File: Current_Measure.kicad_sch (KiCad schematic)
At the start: 4 parts, among them U701 TMCS1101A2UQDT

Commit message: progress on CORE pcb
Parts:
- renumbered C703 to C401, C701 to C402, C702 to C403, U701 to U401
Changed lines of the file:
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@@
 		(on_board yes)
 		(dnp no)
-		(property "Reference" "#PWR0704"
+		(property "Reference" "#PWR0159"
 			(at 157.48 77.47 0)
 			(effects
@@
 			(project "EPS_CORE"
 				(path "/43e5e7c8-e7e0-4528-9a3e-b1557849918d/136d551b-dd5b-42cc-aebd-902cdeeb5d77"
-					(reference "#PWR?")
-					(unit 1)
-				)
-				(path "/43e5e7c8-e7e0-4528-9a3e-b1557849918d/1f66afe8-8069-477a-b3b2-ff8bbac6c1ca"
-					(reference "#PWR?")
+					(reference "#PWR0385")
 					(unit 1)
 				)
 				(path "/43e5e7c8-e7e0-4528-9a3e-b1557849918d/4a53a7b5-59e4-4f40-8227-8276b52a2733"
-					(reference "#PWR?")
+					(reference "#PWR0390")
 					(unit 1)
 				)
 				(path "/43e5e7c8-e7e0-4528-9a3e-b1557849918d/f6059815-62c9-4cb7-94c7-be1aeb1b1210"
-					(reference "#PWR?")
-					(unit 1)
-				)
-				(path "/43e5e7c8-e7e0-4528-9a3e-b1557849918d/f6f0c074-7c68-400b-94dc-3cfae9faea19"
-					(reference "#PWR?")
+					(reference "#PWR0159")
 					(unit 1)
 				)
@@
 		(dnp no)
 		(fields_autoplaced yes)
-		(property "Reference" "#PWR0702"
+		(property "Reference" "#PWR0160"
 			(at 143.51 115.57 0)
 			(effects
@@
 			(project "EPS_CORE"
 				(path "/43e5e7c8-e7e0-4528-9a3e-b1557849918d/136d551b-dd5b-42cc-aebd-902cdeeb5d77"
-					(reference "#PWR?")
-					(unit 1)
-				)
-				(path "/43e5e7c8-e7e0-4528-9a3e-b1557849918d/1f66afe8-8069-477a-b3b2-ff8bbac6c1ca"
-					(reference "#PWR?")
+					(reference "#PWR0386")
 					(unit 1)
 				)
 				(path "/43e5e7c8-e7e0-4528-9a3e-b1557849918d/4a53a7b5-59e4-4f40-8227-8276b52a2733"
-					(reference "#PWR?")
+					(reference "#PWR0391")
 					(unit 1)
 				)
 				(path "/43e5e7c8-e7e0-4528-9a3e-b1557849918d/f6059815-62c9-4cb7-94c7-be1aeb1b1210"
-					(reference "#PWR?")
-					(unit 1)
-				)
-				(path "/43e5e7c8-e7e0-4528-9a3e-b1557849918d/f6f0c074-7c68-400b-94dc-3cfae9faea19"
-					(reference "#PWR?")
+					(reference "#PWR0160")
 					(unit 1)
 				)
@@
 		(on_board yes)
 		(dnp no)
-		(property "Reference" "C701"
+		(property "Reference" "C402"
 			(at 140.97 91.4462 0)
 			(effects
@@
 			(project "EPS_CORE"
 				(path "/43e5e7c8-e7e0-4528-9a3e-b1557849918d/136d551b-dd5b-42cc-aebd-902cdeeb5d77"
-					(reference "C?")
-					(unit 1)
-				)
-				(path "/43e5e7c8-e7e0-4528-9a3e-b1557849918d/1f66afe8-8069-477a-b3b2-ff8bbac6c1ca"
-					(reference "C?")
+					(reference "C1702")
 					(unit 1)
 				)
 				(path "/43e5e7c8-e7e0-4528-9a3e-b1557849918d/4a53a7b5-59e4-4f40-8227-8276b52a2733"
-					(reference "C?")
+					(reference "C1802")
 					(unit 1)
 				)
 				(path "/43e5e7c8-e7e0-4528-9a3e-b1557849918d/f6059815-62c9-4cb7-94c7-be1aeb1b1210"
-					(reference "C?")
-					(unit 1)
-				)
-				(path "/43e5e7c8-e7e0-4528-9a3e-b1557849918d/f6f0c074-7c68-400b-94dc-3cfae9faea19"
-					(reference "C?")
+					(reference "C402")
 					(unit 1)
 				)
@@
 		(dnp no)
 		(fields_autoplaced yes)
-		(property "Reference" "#PWR0705"
+		(property "Reference" "#PWR0162"
 			(at 157.48 110.49 0)
 			(effects
@@
 			(project "EPS_CORE"
 				(path "/43e5e7c8-e7e0-4528-9a3e-b1557849918d/136d551b-dd5b-42cc-aebd-902cdeeb5d77"
-					(reference "#PWR?")
-					(unit 1)
-				)
-				(path "/43e5e7c8-e7e0-4528-9a3e-b1557849918d/1f66afe8-8069-477a-b3b2-ff8bbac6c1ca"
-					(reference "#PWR?")
+					(reference "#PWR0388")
 					(unit 1)
 				)
 				(path "/43e5e7c8-e7e0-4528-9a3e-b1557849918d/4a53a7b5-59e4-4f40-8227-8276b52a2733"
-					(reference "#PWR?")
+					(reference "#PWR0393")
 					(unit 1)
 				)
 				(path "/43e5e7c8-e7e0-4528-9a3e-b1557849918d/f6059815-62c9-4cb7-94c7-be1aeb1b1210"
-					(reference "#PWR?")
-					(unit 1)
-				)
-				(path "/43e5e7c8-e7e0-4528-9a3e-b1557849918d/f6f0c074-7c68-400b-94dc-3cfae9faea19"
-					(reference "#PWR?")
+					(reference "#PWR0162")
 					(unit 1)
 				)
@@
 		(dnp no)
 		(fields_autoplaced yes)
-		(property "Reference" "U701"
+		(property "Reference" "U401"
 			(at 159.6233 81.28 0)
 			(effects
@@
 			(project "EPS_CORE"
 				(path "/43e5e7c8-e7e0-4528-9a3e-b1557849918d/136d551b-dd5b-42cc-aebd-902cdeeb5d77"
-					(reference "U?")
-					(unit 1)
-				)
-				(path "/43e5e7c8-e7e0-4528-9a3e-b1557849918d/1f66afe8-8069-477a-b3b2-ff8bbac6c1ca"
-					(reference "U?")
+					(reference "U1701")
 					(unit 1)
 				)
 				(path "/43e5e7c8-e7e0-4528-9a3e-b1557849918d/4a53a7b5-59e4-4f40-8227-8276b52a2733"
-					(reference "U?")
+					(reference "U1801")
 					(unit 1)
 				)
 				(path "/43e5e7c8-e7e0-4528-9a3e-b1557849918d/f6059815-62c9-4cb7-94c7-be1aeb1b1210"
-					(reference "U?")
-					(unit 1)
-				)
-				(path "/43e5e7c8-e7e0-4528-9a3e-b1557849918d/f6f0c074-7c68-400b-94dc-3cfae9faea19"
-					(reference "U?")
+					(reference "U401")
 					(unit 1)
 				)
@@
 		(on_board yes)
 		(dnp no)
-		(property "Reference" "C703"
+		(property "Reference" "C401"
 			(at 149.86 76.2062 0)
 			(effects
@@
 			(project "EPS_CORE"
 				(path "/43e5e7c8-e7e0-4528-9a3e-b1557849918d/136d551b-dd5b-42cc-aebd-902cdeeb5d77"
-					(reference "C?")
-					(unit 1)
-				)
-				(path "/43e5e7c8-e7e0-4528-9a3e-b1557849918d/1f66afe8-8069-477a-b3b2-ff8bbac6c1ca"
-					(reference "C?")
+					(reference "C1701")
 					(unit 1)
 				)
 				(path "/43e5e7c8-e7e0-4528-9a3e-b1557849918d/4a53a7b5-59e4-4f40-8227-8276b52a2733"
-					(reference "C?")
+					(reference "C1801")
 					(unit 1)
 				)
 				(path "/43e5e7c8-e7e0-4528-9a3e-b1557849918d/f6059815-62c9-4cb7-94c7-be1aeb1b1210"
-					(reference "C?")
-					(unit 1)
-				)
-				(path "/43e5e7c8-e7e0-4528-9a3e-b1557849918d/f6f0c074-7c68-400b-94dc-3cfae9faea19"
-					(reference "C?")
+					(reference "C401")
 					(unit 1)
 				)
@@
 		(on_board yes)
 		(dnp no)
-		(property "Reference" "C702"
+		(property "Reference" "C403"
 			(at 140.97 105.4162 0)
 			(effects
@@
 			(project "EPS_CORE"
 				(path "/43e5e7c8-e7e0-4528-9a3e-b1557849918d/136d551b-dd5b-42cc-aebd-902cdeeb5d77"
-					(reference "C?")
-					(unit 1)
-				)
-				(path "/43e5e7c8-e7e0-4528-9a3e-b1557849918d/1f66afe8-8069-477a-b3b2-ff8bbac6c1ca"
-					(reference "C?")
+					(reference "C1703")
 					(unit 1)
 				)
 				(path "/43e5e7c8-e7e0-4528-9a3e-b1557849918d/4a53a7b5-59e4-4f40-8227-8276b52a2733"
-					(reference "C?")
+					(reference "C1803")
 					(unit 1)
 				)
 				(path "/43e5e7c8-e7e0-4528-9a3e-b1557849918d/f6059815-62c9-4cb7-94c7-be1aeb1b1210"
-					(reference "C?")
-					(unit 1)
-				)
-				(path "/43e5e7c8-e7e0-4528-9a3e-b1557849918d/f6f0c074-7c68-400b-94dc-3cfae9faea19"
-					(reference "C?")
+					(reference "C403")
 					(unit 1)
 				)
@@
 		(dnp no)
 		(fields_autoplaced yes)
-		(property "Reference" "#PWR0701"
+		(property "Reference" "#PWR0161"
 			(at 143.51 101.6 0)
 			(effects
@@
 			(project "EPS_CORE"
 				(path "/43e5e7c8-e7e0-4528-9a3e-b1557849918d/136d551b-dd5b-42cc-aebd-902cdeeb5d77"
-					(reference "#PWR?")
-					(unit 1)
-				)
-				(path "/43e5e7c8-e7e0-4528-9a3e-b1557849918d/1f66afe8-8069-477a-b3b2-ff8bbac6c1ca"
-					(reference "#PWR?")
+					(reference "#PWR0387")
 					(unit 1)
 				)
 				(path "/43e5e7c8-e7e0-4528-9a3e-b1557849918d/4a53a7b5-59e4-4f40-8227-8276b52a2733"
-					(reference "#PWR?")
+					(reference "#PWR0392")
 					(unit 1)
 				)
 				(path "/43e5e7c8-e7e0-4528-9a3e-b1557849918d/f6059815-62c9-4cb7-94c7-be1aeb1b1210"
-					(reference "#PWR?")
-					(unit 1)
-				)
-				(path "/43e5e7c8-e7e0-4528-9a3e-b1557849918d/f6f0c074-7c68-400b-94dc-3cfae9faea19"
-					(reference "#PWR?")
+					(reference "#PWR0161")
 					(unit 1)
 				)
@@
 		(dnp no)
 		(fields_autoplaced yes)
-		(property "Reference" "#PWR0703"
+		(property "Reference" "#PWR0163"
 			(at 152.4 86.36 0)
 			(effects
@@
 			(project "EPS_CORE"
 				(path "/43e5e7c8-e7e0-4528-9a3e-b1557849918d/136d551b-dd5b-42cc-aebd-902cdeeb5d77"
-					(reference "#PWR?")
-					(unit 1)
-				)
-				(path "/43e5e7c8-e7e0-4528-9a3e-b1557849918d/1f66afe8-8069-477a-b3b2-ff8bbac6c1ca"
-					(reference "#PWR?")
+					(reference "#PWR0389")
 					(unit 1)
 				)
 				(path "/43e5e7c8-e7e0-4528-9a3e-b1557849918d/4a53a7b5-59e4-4f40-8227-8276b52a2733"
-					(reference "#PWR?")
+					(reference "#PWR0394")
 					(unit 1)
 				)
 				(path "/43e5e7c8-e7e0-4528-9a3e-b1557849918d/f6059815-62c9-4cb7-94c7-be1aeb1b1210"
-					(reference "#PWR?")
-					(unit 1)
-				)
-				(path "/43e5e7c8-e7e0-4528-9a3e-b1557849918d/f6f0c074-7c68-400b-94dc-3cfae9faea19"
-					(reference "#PWR?")
-					(unit 1)
-				)
+					(reference "#PWR0163")
+					(unit 1)
+				)

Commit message: small changes to test board
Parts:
- renumbered C402 to C701, C403 to C702, C401 to C703, U401 to U701
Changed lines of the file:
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@@
 		(on_board yes)
 		(dnp no)
-		(property "Reference" "#PWR0159"
+		(property "Reference" "#PWR0704"
 			(at 157.48 77.47 0)
 			(effects
@@
 		(dnp no)
 		(fields_autoplaced yes)
-		(property "Reference" "#PWR0160"
+		(property "Reference" "#PWR0702"
 			(at 143.51 115.57 0)
 			(effects
@@
 		(on_board yes)
 		(dnp no)
-		(property "Reference" "C402"
+		(property "Reference" "C701"
 			(at 140.97 91.4462 0)
 			(effects
@@
 		(dnp no)
 		(fields_autoplaced yes)
-		(property "Reference" "#PWR0162"
+		(property "Reference" "#PWR0705"
 			(at 157.48 110.49 0)
 			(effects
@@
 		(dnp no)
 		(fields_autoplaced yes)
-		(property "Reference" "U401"
+		(property "Reference" "U701"
 			(at 159.6233 81.28 0)
 			(effects
@@
 		(on_board yes)
 		(dnp no)
-		(property "Reference" "C401"
+		(property "Reference" "C703"
 			(at 149.86 76.2062 0)
 			(effects
@@
 		(on_board yes)
 		(dnp no)
-		(property "Reference" "C403"
+		(property "Reference" "C702"
 			(at 140.97 105.4162 0)
 			(effects
@@
 		(dnp no)
 		(fields_autoplaced yes)
-		(property "Reference" "#PWR0161"
+		(property "Reference" "#PWR0701"
 			(at 143.51 101.6 0)
 			(effects
@@
 		(dnp no)
 		(fields_autoplaced yes)
-		(property "Reference" "#PWR0163"
+		(property "Reference" "#PWR0703"
 			(at 152.4 86.36 0)
 			(effects

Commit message: nearly finnished CORE pcb
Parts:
- renumbered C703 to C401, C701 to C402, C702 to C403, U701 to U401
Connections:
- net +5V renamed +3V3
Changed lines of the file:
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@@
-	)
-	(symbol
-		(lib_id "power:+5V")
-		(at 157.48 73.66 0)
-		(unit 1)
-		(exclude_from_sim no)
-		(in_bom yes)
-		(on_board yes)
-		(dnp no)
-		(property "Reference" "#PWR0704"
-			(at 157.48 77.47 0)
-			(effects
-				(font
-					(size 1.27 1.27)
-				)
-				(hide yes)
-			)
-		)
-		(property "Value" "+5V"
-			(at 157.48 69.85 0)
-			(effects
-				(font
-					(size 1.27 1.27)
-				)
-			)
-		)
-		(property "Footprint" ""
-			(at 157.48 73.66 0)
-			(effects
-				(font
-					(size 1.27 1.27)
-				)
-				(hide yes)
-			)
-		)
-		(property "Datasheet" ""
-			(at 157.48 73.66 0)
-			(effects
-				(font
-					(size 1.27 1.27)
-				)
-				(hide yes)
-			)
-		)
-		(property "Description" "Power symbol creates a global label with name \"+5V\""
-			(at 157.48 73.66 0)
-			(effects
-				(font
-					(size 1.27 1.27)
-				)
-				(hide yes)
-			)
-		)
-		(pin "1"
-		)
-		(instances
-			(project "TEST_PCB"
-				(path "/29496ace-b476-4f24-a65f-9da1dd70122c/504ee284-c5b3-48b9-b988-a6d19662e437"
-					(reference "#PWR01404")
-					(unit 1)
-				)
-				(path "/29496ace-b476-4f24-a65f-9da1dd70122c/9ac70773-2304-4605-b1e0-d7d1b5f027ba"
-					(reference "#PWR0704")
-					(unit 1)
-				)
-				(path "/29496ace-b476-4f24-a65f-9da1dd70122c/02ad1486-0ecd-4655-9f01-754da17b7441/24296571-f4ee-420c-bcfd-9dd9216b9bef"
-					(reference "#PWR01604")
-					(unit 1)
-				)
-			)
-			(project "EPS_CORE"
-				(path "/43e5e7c8-e7e0-4528-9a3e-b1557849918d/136d551b-dd5b-42cc-aebd-902cdeeb5d77"
-					(reference "#PWR0385")
-					(unit 1)
-				)
-				(path "/43e5e7c8-e7e0-4528-9a3e-b1557849918d/4a53a7b5-59e4-4f40-8227-8276b52a2733"
-					(reference "#PWR0390")
-					(unit 1)
-				)
-				(path "/43e5e7c8-e7e0-4528-9a3e-b1557849918d/f6059815-62c9-4cb7-94c7-be1aeb1b1210"
-					(reference "#PWR0159")
-					(unit 1)
-				)
-			)
-			(project "EPS"
-				(path "/94201994-47b8-4213-8d1a-05da12b2a7b0/2939b268-15b7-411b-af55-ccc6daa126bc/3652e430-ea4c-4576-9fde-9d6a5c3d8e65"
-					(reference "#PWR03404")
-					(unit 1)
-				)
-				(path "/94201994-47b8-4213-8d1a-05da12b2a7b0/2939b268-15b7-411b-af55-ccc6daa126bc/544fbc8e-c1c2-4d03-8c38-2510c623901a"
-					(reference "#PWR04304")
-					(unit 1)
-				)
-				(path "/94201994-47b8-4213-8d1a-05da12b2a7b0/2939b268-15b7-411b-af55-ccc6daa126bc/a13b3f6b-9de9-421b-abab-aef62fcea990"
-					(reference "#PWR03304")
-					(unit 1)
-				)
-				(path "/94201994-47b8-4213-8d1a-05da12b2a7b0/2939b268-15b7-411b-af55-ccc6daa126bc/f63c6608-9a95-45da-aef6-1346c5385a30"
-					(reference "#PWR03504")
-					(unit 1)
-				)
-				(path "/94201994-47b8-4213-8d1a-05da12b2a7b0/447ec425-294e-4947-a7f3-941020b4706e/136d551b-dd5b-42cc-aebd-902cdeeb5d77"
-					(reference "#PWR05104")
-					(unit 1)
-				)
-				(path "/94201994-47b8-4213-8d1a-05da12b2a7b0/447ec425-294e-4947-a7f3-941020b4706e/4a53a7b5-59e4-4f40-8227-8276b52a2733"
-					(reference "#PWR05204")
-					(unit 1)
-				)
-				(path "/94201994-47b8-4213-8d1a-05da12b2a7b0/447ec425-294e-4947-a7f3-941020b4706e/f6059815-62c9-4cb7-94c7-be1aeb1b1210"
-					(reference "#PWR05604")
-					(unit 1)
-				)
-				(path "/94201994-47b8-4213-8d1a-05da12b2a7b0/c37f0a0b-f6f4-4c63-8ce8-6ee6766e791f/41c5534f-fcb2-4ec3-adc7-992b7bee1600/24296571-f4ee-420c-bcfd-9dd9216b9bef"
-					(reference "#PWR01404")
-					(unit 1)
-				)
-				(path "/94201994-47b8-4213-8d1a-05da12b2a7b0/c37f0a0b-f6f4-4c63-8ce8-6ee6766e791f/4313468d-8f4f-4bdc-8385-889814f4cee5/24296571-f4ee-420c-bcfd-9dd9216b9bef"
-					(reference "#PWR0604")
-					(unit 1)
-				)
-				(path "/94201994-47b8-4213-8d1a-05da12b2a7b0/c37f0a0b-f6f4-4c63-8ce8-6ee6766e791f/52873e6b-e08e-4161-9ef2-2b4737346b9b/24296571-f4ee-420c-bcfd-9dd9216b9bef"
-					(reference "#PWR01804")
-					(unit 1)
-				)
-				(path "/94201994-47b8-4213-8d1a-05da12b2a7b0/c37f0a0b-f6f4-4c63-8ce8-6ee6766e791f/65753da0-d365-4e1b-a747-1fe94f193180/24296571-f4ee-420c-bcfd-9dd9216b9bef"
-					(reference "#PWR02204")
-					(unit 1)
-				)
-				(path "/94201994-47b8-4213-8d1a-05da12b2a7b0/c37f0a0b-f6f4-4c63-8ce8-6ee6766e791f/6d13a628-cc69-4882-8d71-6117aca3a662/24296571-f4ee-420c-bcfd-9dd9216b9bef"
-					(reference "#PWR01004")
-					(unit 1)
-				)
-				(path "/94201994-47b8-4213-8d1a-05da12b2a7b0/c37f0a0b-f6f4-4c63-8ce8-6ee6766e791f/9d09256a-b1cf-431e-ac15-ed14acab8c88/24296571-f4ee-420c-bcfd-9dd9216b9bef"
-					(reference "#PWR0304")
-					(unit 1)
-				)
-			)
-		)
 	)
 	(symbol
@@
 		(dnp no)
 		(fields_autoplaced yes)
-		(property "Reference" "#PWR0702"
+		(property "Reference" "#PWR0160"
 			(at 143.51 115.57 0)
 			(effects
@@
 		(on_board yes)
 		(dnp no)
-		(property "Reference" "C701"
+		(property "Reference" "C402"
 			(at 140.97 91.4462 0)
 			(effects
@@
 		(dnp no)
 		(fields_autoplaced yes)
-		(property "Reference" "#PWR0705"
+		(property "Reference" "#PWR0162"
 			(at 157.48 110.49 0)
 			(effects
@@
 		(dnp no)
 		(fields_autoplaced yes)
-		(property "Reference" "U701"
+		(property "Reference" "U401"
 			(at 159.6233 81.28 0)
 			(effects
@@
 		(on_board yes)
 		(dnp no)
-		(property "Reference" "C703"
+		(property "Reference" "C401"
 			(at 149.86 76.2062 0)
 			(effects
@@
 		(on_board yes)
 		(dnp no)
-		(property "Reference" "C702"
+		(property "Reference" "C403"
 			(at 140.97 105.4162 0)
 			(effects
@@
 		(dnp no)
 		(fields_autoplaced yes)
-		(property "Reference" "#PWR0701"
+		(property "Reference" "#PWR0161"
 			(at 143.51 101.6 0)
 			(effects
@@
 		(dnp no)
 		(fields_autoplaced yes)
-		(property "Reference" "#PWR0703"
+		(property "Reference" "#PWR0163"
 			(at 152.4 86.36 0)
 			(effects
@@
 					(unit 1)
 				)
+			)
+		)
+	)
+	(symbol
+		(lib_id "power:+3V3")
+		(at 157.48 73.66 0)
+		(unit 1)
+		(exclude_from_sim no)
+		(in_bom yes)
+		(on_board yes)
+		(dnp no)
+		(fields_autoplaced yes)
+		(property "Reference" "#PWR0401"
+			(at 157.48 77.47 0)
+			(effects
+				(font
+					(size 1.27 1.27)
+				)
+				(hide yes)
+			)
+		)
+		(property "Value" "+3V3"
+			(at 157.48 68.58 0)
+			(effects
+				(font
+					(size 1.27 1.27)
+				)
+			)
+		)
+		(property "Footprint" ""
+			(at 157.48 73.66 0)
+			(effects
+				(font
+					(size 1.27 1.27)
+				)
+				(hide yes)
+			)
+		)
+		(property "Datasheet" ""
+			(at 157.48 73.66 0)
+			(effects
+				(font
+					(size 1.27 1.27)
+				)
+				(hide yes)
+			)
+		)
+		(property "Description" "Power symbol creates a global label with name \"+3V3\""
+			(at 157.48 73.66 0)
+			(effects
+				(font
+					(size 1.27 1.27)
+				)
+				(hide yes)
+			)
+		)
+		(pin "1"
+		)
+		(instances
+			(project ""
+				(path "/43e5e7c8-e7e0-4528-9a3e-b1557849918d/136d551b-dd5b-42cc-aebd-902cdeeb5d77"
+					(reference "#PWR01701")
+					(unit 1)
+				)
+				(path "/43e5e7c8-e7e0-4528-9a3e-b1557849918d/4a53a7b5-59e4-4f40-8227-8276b52a2733"
+					(reference "#PWR01801")
+					(unit 1)
+				)
+				(path "/43e5e7c8-e7e0-4528-9a3e-b1557849918d/f6059815-62c9-4cb7-94c7-be1aeb1b1210"
+					(reference "#PWR0401")
+					(unit 1)
+				)

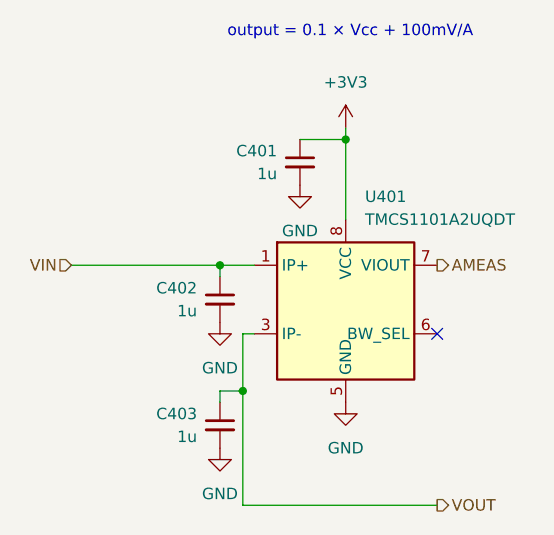
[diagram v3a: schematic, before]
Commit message: pcb progres for all components
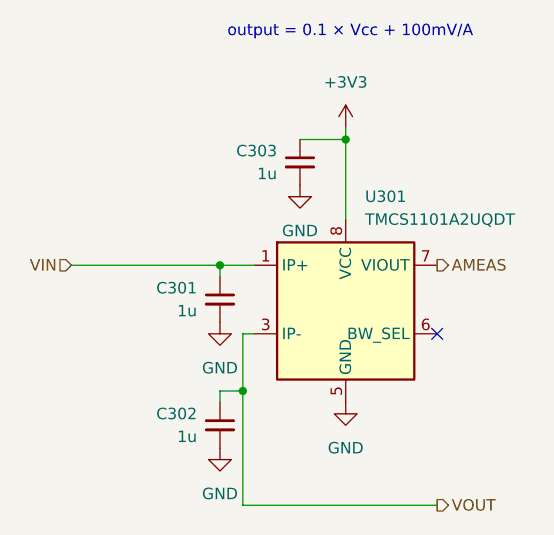
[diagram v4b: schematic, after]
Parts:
- renumbered C402 to C301, C403 to C302, C401 to C303, U401 to U301

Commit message: progress on PCBs
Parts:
- renumbered C303 to C1501, C301 to C1502, C302 to C1503, U301 to U1501
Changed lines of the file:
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@@
 		(dnp no)
 		(fields_autoplaced yes)
-		(property "Reference" "#PWR0302"
+		(property "Reference" "#PWR01505"
 			(at 143.51 115.57 0)
 			(effects
@@
 		(on_board yes)
 		(dnp no)
-		(property "Reference" "C301"
+		(property "Reference" "C1502"
 			(at 140.97 91.4462 0)
 			(effects
@@
 		(dnp no)
 		(fields_autoplaced yes)
-		(property "Reference" "#PWR0305"
+		(property "Reference" "#PWR01504"
 			(at 157.48 110.49 0)
 			(effects
@@
 		(dnp no)
 		(fields_autoplaced yes)
-		(property "Reference" "U301"
+		(property "Reference" "U1501"
 			(at 159.6233 81.28 0)
 			(effects
@@
 		(on_board yes)
 		(dnp no)
-		(property "Reference" "C303"
+		(property "Reference" "C1501"
 			(at 149.86 76.2062 0)
 			(effects
@@
 		(on_board yes)
 		(dnp no)
-		(property "Reference" "C302"
+		(property "Reference" "C1503"
 			(at 140.97 105.4162 0)
 			(effects
@@
 		(dnp no)
 		(fields_autoplaced yes)
-		(property "Reference" "#PWR0301"
+		(property "Reference" "#PWR01503"
 			(at 143.51 101.6 0)
 			(effects
@@
 		(dnp no)
 		(fields_autoplaced yes)
-		(property "Reference" "#PWR0303"
+		(property "Reference" "#PWR01502"
 			(at 152.4 86.36 0)
 			(effects
@@
 		(dnp no)
 		(fields_autoplaced yes)
-		(property "Reference" "#PWR?"
+		(property "Reference" "#PWR01501"
 			(at 157.48 77.47 0)
 			(effects
